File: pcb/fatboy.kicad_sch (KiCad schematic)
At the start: 78 parts, among them J1 Conn_01x04, SW1 SW_Push, U1 Helios

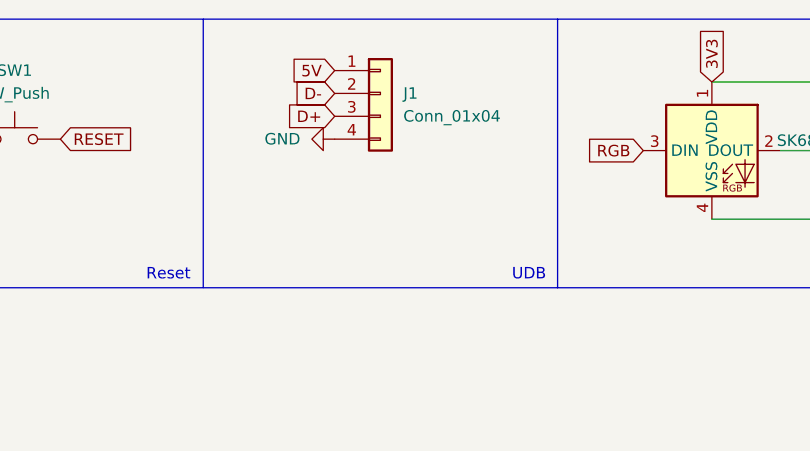
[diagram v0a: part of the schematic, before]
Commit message: sch: remove daughterboard
Signed-off-by: Anant Thazhemadam <anant.thazhemadam@gmail.com>
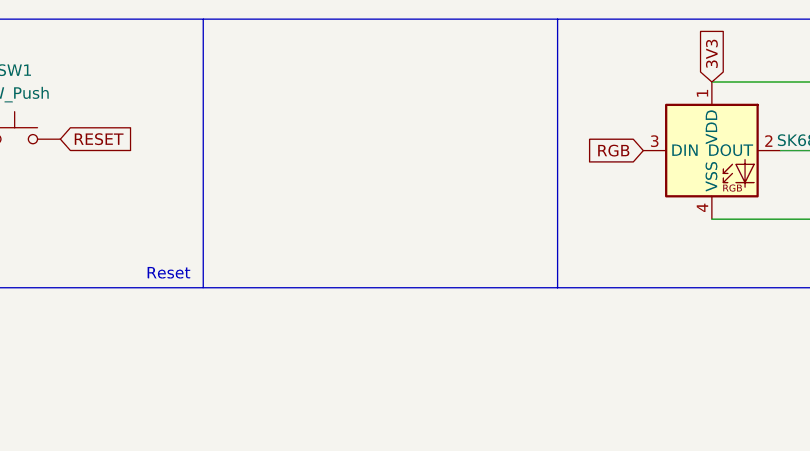
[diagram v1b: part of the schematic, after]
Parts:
- removed J1: Conn_01x04, fatboy:Molex_Pico-EZmate_78171-0004_1x04-1MP_P1.20mm_Vertical, symbol Connector_Generic:Conn_01x04
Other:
- note removed: "UDB"
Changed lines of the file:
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@@
 		)
 	)
-	(text "UDB"
-		(exclude_from_sim no)
-		(at 137.795 41.91 0)
-		(effects
-			(font
-				(size 1.27 1.27)
-			)
-			(justify left bottom)
-		)
-	)
 	(text "Diode Matrix"
 		(exclude_from_sim no)
@@
 		)
 	)
-	(global_label "D+"
-		(shape input)
-		(at 118.11 23.495 180)
-		(fields_autoplaced yes)
-		(effects
-			(font
-				(size 1.27 1.27)
-			)
-			(justify right)
-		)
-		(property "Intersheetrefs" "${INTERSHEET_REFS}"
-			(at 112.2824 23.495 0)
-			(effects
-				(font
-					(size 1.27 1.27)
-				)
-				(justify right)
-				(hide yes)
-			)
-		)
-	)
 	(global_label "ROW2"
 		(shape input)
@@
 		)
 	)
-	(global_label "D-"
-		(shape input)
-		(at 118.11 20.955 180)
-		(fields_autoplaced yes)
-		(effects
-			(font
-				(size 1.27 1.27)
-			)
-			(justify right)
-		)
-		(property "Intersheetrefs" "${INTERSHEET_REFS}"
-			(at 112.2824 20.955 0)
-			(effects
-				(font
-					(size 1.27 1.27)
-				)
-				(justify right)
-				(hide yes)
-			)
-		)
-	)
 	(global_label "COL8"
 		(shape input)
@@
 		)
 	)
-	(global_label "5V"
-		(shape input)
-		(at 118.11 18.415 180)
-		(fields_autoplaced yes)
-		(effects
-			(font
-				(size 1.27 1.27)
-			)
-			(justify right)
-		)
-		(property "Intersheetrefs" "${INTERSHEET_REFS}"
-			(at 112.8267 18.415 0)
-			(effects
-				(font
-					(size 1.27 1.27)
-				)
-				(justify right)
-				(hide yes)
-			)
-		)
-	)
 	(global_label "D-"
 		(shape input)
@@
 	)
 	(symbol
-		(lib_id "power:GND")
-		(at 118.11 26.035 270)
-		(unit 1)
-		(exclude_from_sim no)
-		(in_bom yes)
-		(on_board yes)
-		(dnp no)
-		(fields_autoplaced yes)
-		(property "Reference" "#PWR05"
-			(at 111.76 26.035 0)
-			(effects
-				(font
-					(size 1.27 1.27)
-				)
-				(hide yes)
-			)
-		)
-		(property "Value" "GND"
-			(at 114.3 26.035 90)
-			(effects
-				(font
-					(size 1.27 1.27)
-				)
-				(justify right)
-			)
-		)
-		(property "Footprint" ""
-			(at 118.11 26.035 0)
-			(effects
-				(font
-					(size 1.27 1.27)
-				)
-				(hide yes)
-			)
-		)
-		(property "Datasheet" ""
-			(at 118.11 26.035 0)
-			(effects
-				(font
-					(size 1.27 1.27)
-				)
-				(hide yes)
-			)
-		)
-		(property "Description" ""
-			(at 118.11 26.035 0)
-			(effects
-				(font
-					(size 1.27 1.27)
-				)
-				(hide yes)
-			)
-		)
-		(pin "1"
-		)
-		(instances
-			(project "fatboy"
-				(path "/ebfc642c-0c68-4d3e-b71f-85668561aa10"
-					(reference "#PWR05")
-					(unit 1)
-				)
-			)
-		)
-	)
-	(symbol
 		(lib_id "Diode:1N4148W")
 		(at 44.45 129.54 90)
@@
 					(unit 1)
 				)
-			)
-		)
-	)
-	(symbol
-		(lib_id "Connector_Generic:Conn_01x04")
-		(at 123.19 20.955 0)
-		(unit 1)
-		(exclude_from_sim no)
-		(in_bom yes)
-		(on_board yes)
-		(dnp no)
-		(fields_autoplaced yes)
-		(property "Reference" "J1"
-			(at 125.73 20.955 0)
-			(effects
-				(font
-					(size 1.27 1.27)
-				)
-				(justify left)
-			)
-		)
-		(property "Value" "Conn_01x04"
-			(at 125.73 23.495 0)
-			(effects
-				(font
-					(size 1.27 1.27)
-				)
-				(justify left)
-			)
-		)
-		(property "Footprint" "fatboy:Molex_Pico-EZmate_78171-0004_1x04-1MP_P1.20mm_Vertical"
-			(at 123.19 20.955 0)
-			(effects
-				(font
-					(size 1.27 1.27)
-				)
-				(hide yes)
-			)
-		)
-		(property "Datasheet" "~"
-			(at 123.19 20.955 0)
-			(effects
-				(font
-					(size 1.27 1.27)
-				)
-				(hide yes)
-			)
-		)
-		(property "Description" ""
-			(at 123.19 20.955 0)
-			(effects
-				(font
-					(size 1.27 1.27)
-				)
-				(hide yes)
-			)
-		)
-		(pin "1"
-		)
-		(pin "2"
-		)
-		(pin "4"
-		)
-		(pin "3"
-		)
-		(instances
-			(project "fatboy"
-				(path "/ebfc642c-0c68-4d3e-b71f-85668561aa10"
-					(reference "J1")
-					(unit 1)
-				)

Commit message: sch: update symbols from library
Signed-off-by: Anant Thazhemadam <anant.thazhemadam@gmail.com>
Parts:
- D1, D10, D11, D12, D13, D14, D15, D16, D17, D18, D19, D2, D20, D21, D22, D23, D24, D25, D26, D27, D28, D29, D3, D30, D31, D32, D33, D34, D35, D36, D4, D5, D6, D7, D8, D9: footprint fatboy:D_SOD-123 -> Diode_SMD:D_SOD-123
- LED1, LED2, LED3: footprint fatboy:LED_6028R -> PCM_marbastlib-various:LED_6028R
- MX1, MX10, MX11, MX12, MX13, MX14, MX15, MX16, MX17, MX18, MX19, MX2, MX20, MX21, MX22, MX23, MX24, MX25, MX26, MX27, MX28, MX29, MX3, MX30, MX31, MX32, MX33, MX34, MX35, MX36, MX4, MX5, MX6, MX7, MX8, MX9: footprint fatboy:SW_MX_HS_1u -> PCM_marbastlib-mx:SW_MX_HS_1u
- U1: footprint fatboy:Helios_ACH -> PCM_marbastlib-xp-promicroish:Helios_AH_USBup

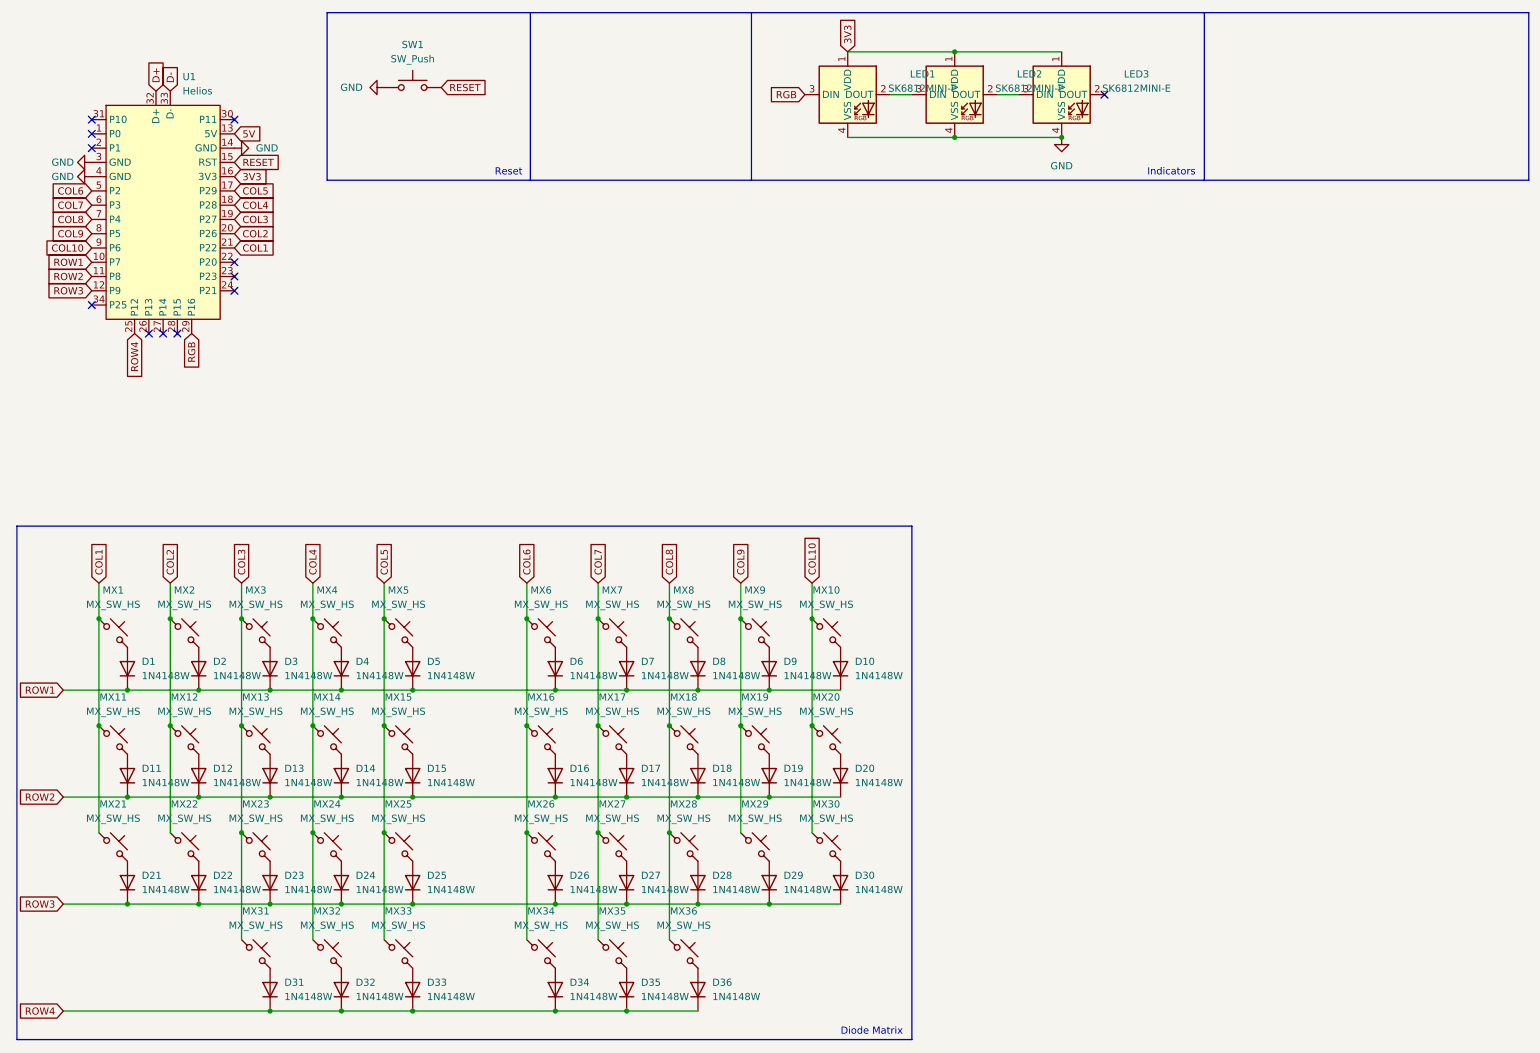
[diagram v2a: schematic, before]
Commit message: sch: remove extra led
Signed-off-by: Anant Thazhemadam <anant.thazhemadam@gmail.com>
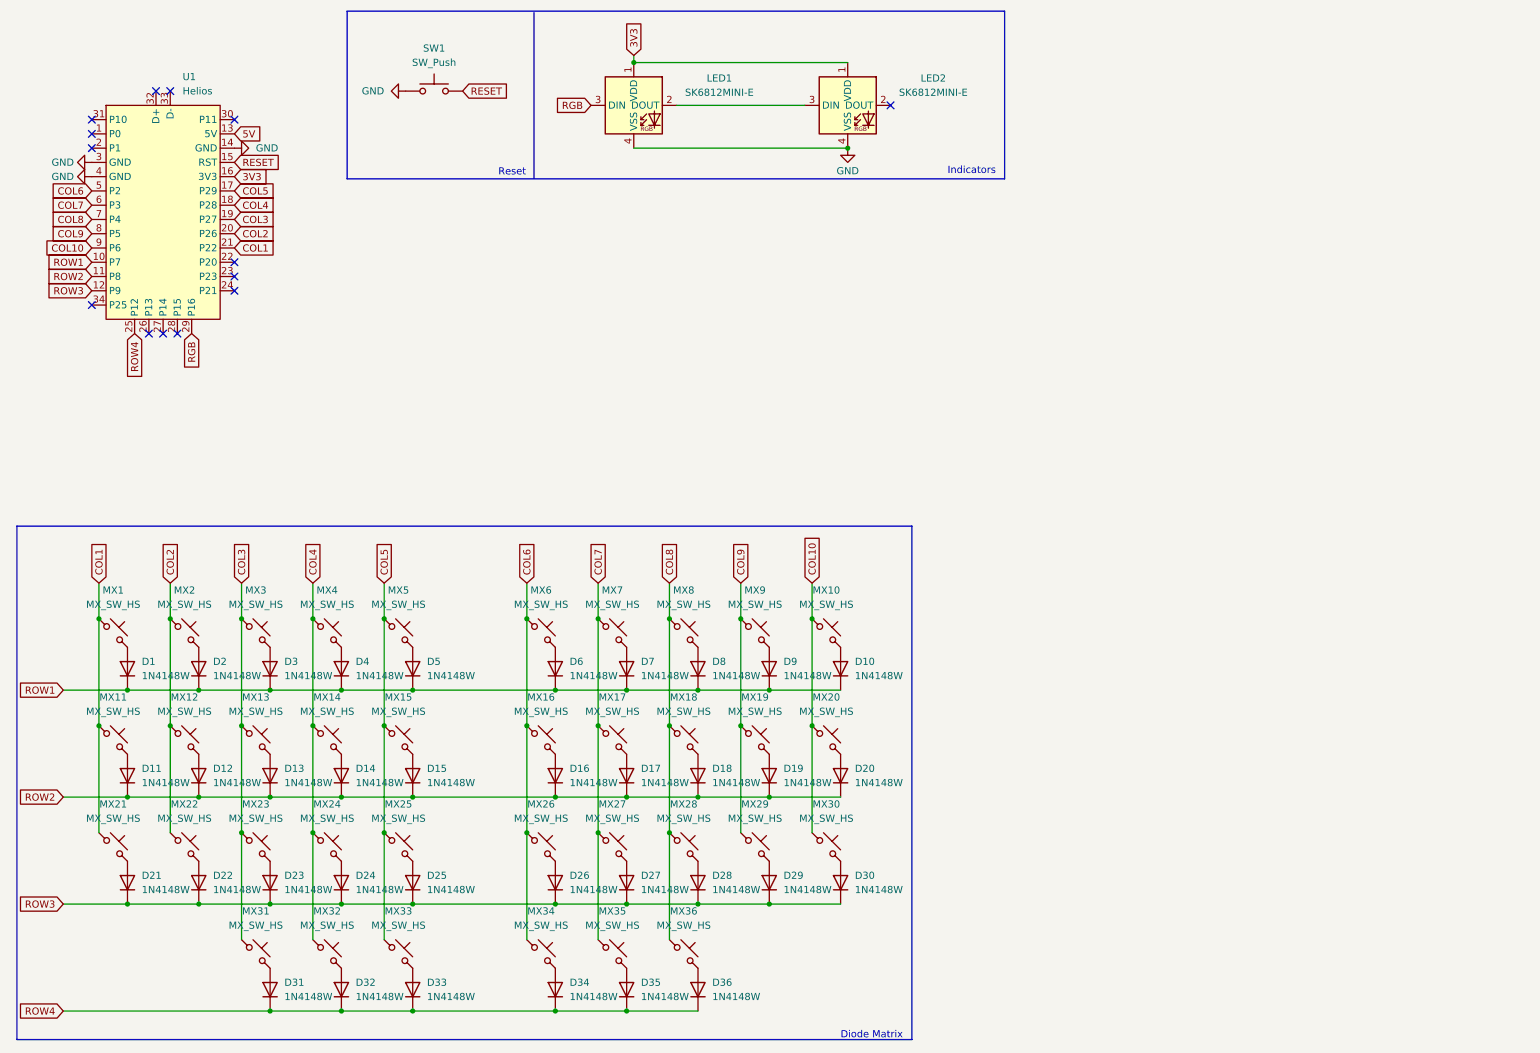
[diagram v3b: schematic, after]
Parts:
- removed LED3: SK6812MINI-E, PCM_marbastlib-various:LED_6028R, symbol marbastlib-various:SK6812MINI-E
- D1, D10, D11, D12, D13, D14, D15, D16, D17, D18, D19, D2, D20, D21, D22, D23, D24, D25, D26, D27, D28, D29, D3, D30, D31, D32, D33, D34, D35, D36, D4, D5, D6, D7, D8, D9: footprint Diode_SMD:D_SOD-123 -> fatboy:D_SOD-123
- LED1, LED2: footprint PCM_marbastlib-various:LED_6028R -> fatboy:LED_6028R
- MX1, MX10, MX11, MX12, MX13, MX14, MX15, MX16, MX17, MX18, MX19, MX2, MX20, MX21, MX22, MX23, MX24, MX25, MX26, MX27, MX28, MX29, MX3, MX30, MX31, MX32, MX33, MX34, MX35, MX36, MX4, MX5, MX6, MX7, MX8, MX9: footprint PCM_marbastlib-mx:SW_MX_HS_1u -> fatboy:SW_MX_HS_1u
- U1: footprint PCM_marbastlib-xp-promicroish:Helios_AH_USBup -> fatboy:Helios_ACH
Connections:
- net D+: no longer names the net of U1.32 (D+)
- net D-: no longer names the net of U1.33 (D-)
- no-connect marks 12 -> 14
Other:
- moved on the sheet: LED1, LED2, SW1

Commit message: sch: update diode symbols
Signed-off-by: Anant Thazhemadam <anant.thazhemadam@gmail.com>
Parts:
- D1, D10, D11, D12, D13, D14, D15, D16, D17, D18, D19, D2, D20, D21, D22, D23, D24, D25, D26, D27, D28, D29, D3, D30, D31, D32, D33, D34, D35, D36, D4, D5, D6, D7, D8, D9: footprint fatboy:D_SOD-123 -> Diode_SMD:D_SOD-123

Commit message: update MX HS SW footprint to PCM_marbastlib-mx:SW_MX_HS_CPG151101S11_1u
Signed-off-by: Anant Thazhemadam <anant.thazhemadam@gmail.com>
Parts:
- removed MX1, MX10, MX11, MX12, MX13, MX14, MX15, MX16, MX17, MX18, MX19, MX2, MX20, MX21, MX22, MX23, MX24, MX25, MX26, MX27, MX28, MX29, MX3, MX30, MX31, MX32, MX33, MX34, MX35, MX36, MX4, MX5, MX6, MX7, MX8, MX9: MX_SW_HS, fatboy:SW_MX_HS_1u, symbol marbastlib-mx:MX_SW_HS
- added MX1, MX10, MX11, MX12, MX13, MX14, MX15, MX16, MX17, MX18, MX19, MX2, MX20, MX21, MX22, MX23, MX24, MX25, MX26, MX27, MX28, MX29, MX3, MX30, MX31, MX32, MX33, MX34, MX35, MX36, MX4, MX5, MX6, MX7, MX8, MX9: MX_SW_HS, PCM_marbastlib-mx:SW_MX_HS_CPG151101S11_1u, symbol PCM_marbastlib-mx:MX_SW_HS_CPG151101S11
- U1: footprint fatboy:Helios_ACH -> PCM_marbastlib-xp-promicroish:Helios_ACH
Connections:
- net COL1: now also MX1.1, MX11.1, MX21.1
- net COL10: now also MX10.1, MX20.1, MX30.1
- net COL2: now also MX12.1, MX2.1, MX22.1
- net COL3: now also MX13.1, MX23.1, MX3.1, MX31.1
- net COL4: now also MX14.1, MX24.1, MX32.1, MX4.1
- net COL5: now also MX15.1, MX25.1, MX33.1, MX5.1
- net COL6: now also MX16.1, MX26.1, MX34.1, MX6.1
- net COL7: now also MX17.1, MX27.1, MX35.1, MX7.1
- net COL8: now also MX18.1, MX28.1, MX36.1, MX8.1
- net COL9: now also MX19.1, MX29.1, MX9.1
- net at D6.2 (A): now also MX6.2
- net at D2.2 (A): now also MX2.2
- net at D4.2 (A): now also MX4.2
- net at D15.2 (A): now also MX15.2
- net at D14.2 (A): now also MX14.2
- net at D11.2 (A): now also MX11.2
- net at D18.2 (A): now also MX18.2
- net at D36.2 (A): now also MX36.2
- net at D27.2 (A): now also MX27.2
- net at D8.2 (A): now also MX8.2
- net at D34.2 (A): now also MX34.2
- net at D1.2 (A): now also MX1.2
- net at D12.2 (A): now also MX12.2
- net at D13.2 (A): now also MX13.2
- net at D17.2 (A): now also MX17.2
- net at D26.2 (A): now also MX26.2
- net at D31.2 (A): now also MX31.2
- net at D20.2 (A): now also MX20.2
- net at D16.2 (A): now also MX16.2
- net at D25.2 (A): now also MX25.2
- net at D33.2 (A): now also MX33.2
- net at D5.2 (A): now also MX5.2
- net at D10.2 (A): now also MX10.2
- net at D28.2 (A): now also MX28.2
- net at D9.2 (A): now also MX9.2
- net at D3.2 (A): now also MX3.2
- net at D32.2 (A): now also MX32.2
- net at D22.2 (A): now also MX22.2
- net at D29.2 (A): now also MX29.2
- net at D24.2 (A): now also MX24.2
- net at D30.2 (A): now also MX30.2
- net at D19.2 (A): now also MX19.2
- net at D35.2 (A): now also MX35.2
- net at D21.2 (A): now also MX21.2
- net at D23.2 (A): now also MX23.2
- net at D7.2 (A): now also MX7.2
